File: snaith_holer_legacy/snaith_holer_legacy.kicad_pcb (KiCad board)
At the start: 2 copper layers, 30 x 30 mm, 24 parts, among them J1 Conn_02x08_Odd_Even, J10 Conn_01x01, J11 Conn_01x01, J12 Conn_01x01, J13 Conn_01x01, J14 Conn_01x01, J15 Conn_01x01, J16 Conn_01x01, J17 Conn_01x01, J18 Conn_01x01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

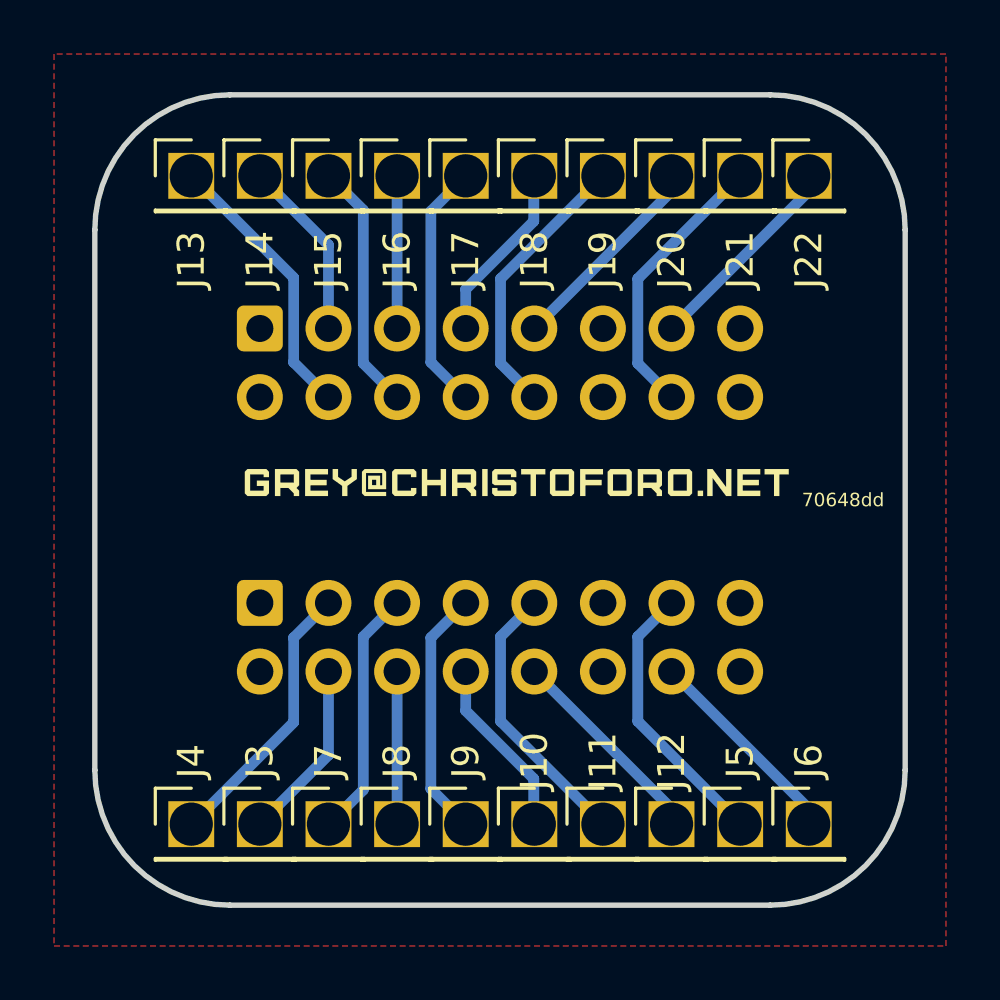
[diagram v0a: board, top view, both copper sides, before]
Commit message: make legacy substrate adapter pcbs
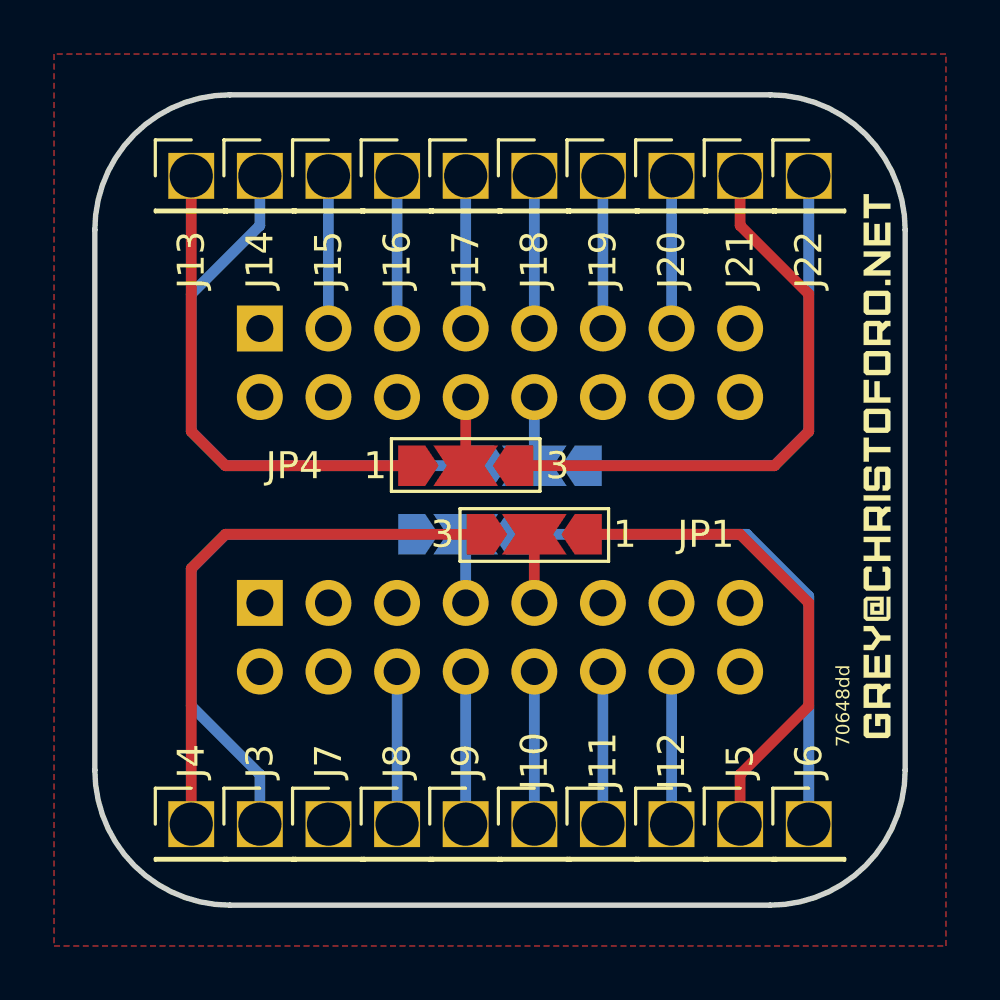
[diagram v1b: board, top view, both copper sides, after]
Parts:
- added JP1: SolderJumper_3_Bridged123, Jumper:SolderJumper-3_P2.0mm_Open_TrianglePad1.0x1.5mm_NumberLabels, F.Cu at (143.3, 95.4)
- added JP2: SolderJumper_3_Bridged123, Jumper:SolderJumper-3_P2.0mm_Open_TrianglePad1.0x1.5mm_NumberLabels, B.Cu at (140.7, 95.4)
- added JP3: SolderJumper_3_Bridged123, Jumper:SolderJumper-3_P2.0mm_Open_TrianglePad1.0x1.5mm_NumberLabels, B.Cu at (143.3, 92.9)
- added JP4: SolderJumper_3_Bridged123, Jumper:SolderJumper-3_P2.0mm_Open_TrianglePad1.0x1.5mm_NumberLabels, F.Cu at (140.7, 92.9)
- J1, J2: footprint custom:HIF3FC-16PA-2.54DSA(71) -> Connector_PinHeader_2.54mm:PinHeader_2x08_P2.54mm_Vertical
- moved SYM1 13.4 mm to (156.0, 92.9), turned to 90 degrees
- moved SYM2 13.4 mm to (156.0, 92.9), turned to 90 degrees
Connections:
- J1 pad 10: /V_5 -> /V_3
- J1 pad 12: unconnected-(J1-Pin_12-Pad12) -> /I_5
- J1 pad 13: /I_OD_B -> unconnected-(J1-Pin_13-Pad13)
- J1 pad 14: /V_OD_B -> /V_5
- J1 pad 3: /I_OD_T -> unconnected-(J1-Pin_3-Pad3)
- J1 pad 4: /V_OD_T -> /I_1
- J1 pad 5: /I_1 -> unconnected-(J1-Pin_5-Pad5)
- J1 pad 7: /I_3 -> /VB
- J1 pad 8: /V_3 -> /I_3
- J1 pad 9: /I_5 -> /IB
- J2 pad 10: /V_6 -> /IT
- J2 pad 11: unconnected-(J2-Pin_11-Pad11) -> /V_6
- J2 pad 13: /I_EV_B -> /I_6
- J2 pad 14: /V_EV_B -> unconnected-(J2-Pin_14-Pad14)
- J2 pad 3: /I_EV_T -> /V_2
- J2 pad 4: /V_EV_T -> unconnected-(J2-Pin_4-Pad4)
- J2 pad 6: /V_2 -> unconnected-(J2-Pin_6-Pad6)
- J2 pad 7: /I_4 -> /V_4
- J2 pad 8: /V_4 -> /VT
- J2 pad 9: /I_6 -> /I_4
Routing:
- net /I_EV_T: track 6.71 -> 21.7 mm
- net /V_OD_T: track 6.71 -> 19.2 mm
- net /V_OD_B: track 7.75 -> 20.1 mm
- net /V_EV_B: track 10.3 -> 21.7 mm
- net /I_OD_T: track 10.3 -> 20.7 mm
- net /I_EV_B: track 7.75 -> 18.1 mm
- net /I_1: track 9.23 -> 0.00 mm
- net /I_OD_B: track 10.3 -> 18.5 mm
- net /V_EV_T: track 10.3 -> 18.1 mm
- net /V_6: track 10.3 -> 5.65 mm
- net /I_5: track 10.3 -> 5.65 mm
- net /V_4: track 9.27 -> 5.65 mm
- net /I_3: track 9.27 -> 5.65 mm
- net /V_2: track 9.23 -> 5.65 mm
- net /VT: track 0.00 -> 2.54 mm
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
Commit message: upgrade contact checker with sense circuitry
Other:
- board text added: "0fe0217"
- board text removed: "70648dd"
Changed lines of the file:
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@@
     (effects (font (size 1 1) (thickness 0.15)) (justify mirror))
   )
-  (gr_text "70648dd" (at 154.7 101.76 90) (layer "B.SilkS")
+  (gr_text "0fe0217" (at 154.7 101.76 90) (layer "B.SilkS")
     (effects (font (size 0.5 0.5) (thickness 0.0625)) (justify mirror))
   )
@@
     (effects (font (size 1 1) (thickness 0.15)) (justify mirror))
   )
-  (gr_text "70648dd" (at 154.7 101.76 90) (layer "F.SilkS")
+  (gr_text "0fe0217" (at 154.7 101.76 90) (layer "F.SilkS")
     (effects (font (size 0.5 0.5) (thickness 0.0625)))
   )

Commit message: add some missing silkscreen
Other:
- board text added: "77a6489"
- board text removed: "0fe0217"
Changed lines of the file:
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@@
     (effects (font (size 1 1) (thickness 0.15)) (justify mirror))
   )
-  (gr_text "0fe0217" (at 154.7 101.76 90) (layer "B.SilkS")
-    (effects (font (size 0.5 0.5) (thickness 0.0625)) (justify mirror))
+  (gr_text "77a6489" (at 128.665 94.14 -90) (layer "B.SilkS")
+    (effects (font (size 1.5 1.5) (thickness 0.3) bold) (justify mirror))
   )
   (gr_text "2" (at 136.92 80.17 180) (layer "B.SilkS")
@@
     (effects (font (size 1 1) (thickness 0.15)) (justify mirror))
   )
-  (gr_text "0fe0217" (at 154.7 101.76 90) (layer "F.SilkS")
-    (effects (font (size 0.5 0.5) (thickness 0.0625)))
+  (gr_text "77a6489" (at 128.665 94.14 90) (layer "F.SilkS")
+    (effects (font (size 1.5 1.5) (thickness 0.3) bold))
   )
   (segment (start 130.57 106.14) (end 130.57 96.68) (width 0.4) (layer "F.Cu") (net 1))

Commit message: update silk
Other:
- board text added: "c5b4c2a"
- board text removed: "77a6489"
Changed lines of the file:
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@@
     (effects (font (size 1 1) (thickness 0.15)) (justify mirror))
   )
-  (gr_text "77a6489" (at 128.665 94.14 -90) (layer "B.SilkS")
+  (gr_text "c5b4c2a" (at 128.665 94.14 270) (layer "B.SilkS")
     (effects (font (size 1.5 1.5) (thickness 0.3) bold) (justify mirror))
   )
@@
     (effects (font (size 1 1) (thickness 0.15)) (justify mirror))
   )
-  (gr_text "77a6489" (at 128.665 94.14 90) (layer "F.SilkS")
+  (gr_text "c5b4c2a" (at 128.665 94.14 90) (layer "F.SilkS")
     (effects (font (size 1.5 1.5) (thickness 0.3) bold))
   )

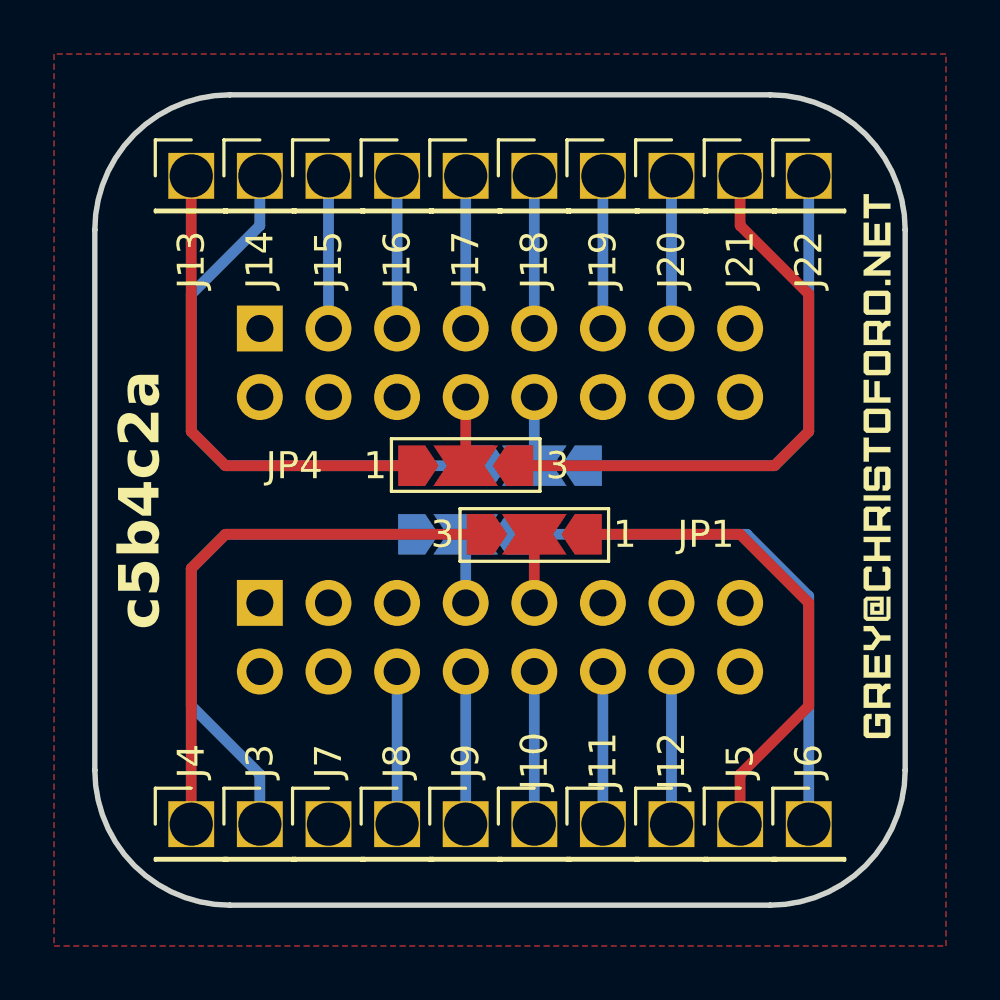
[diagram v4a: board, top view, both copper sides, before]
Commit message: fix missing trace
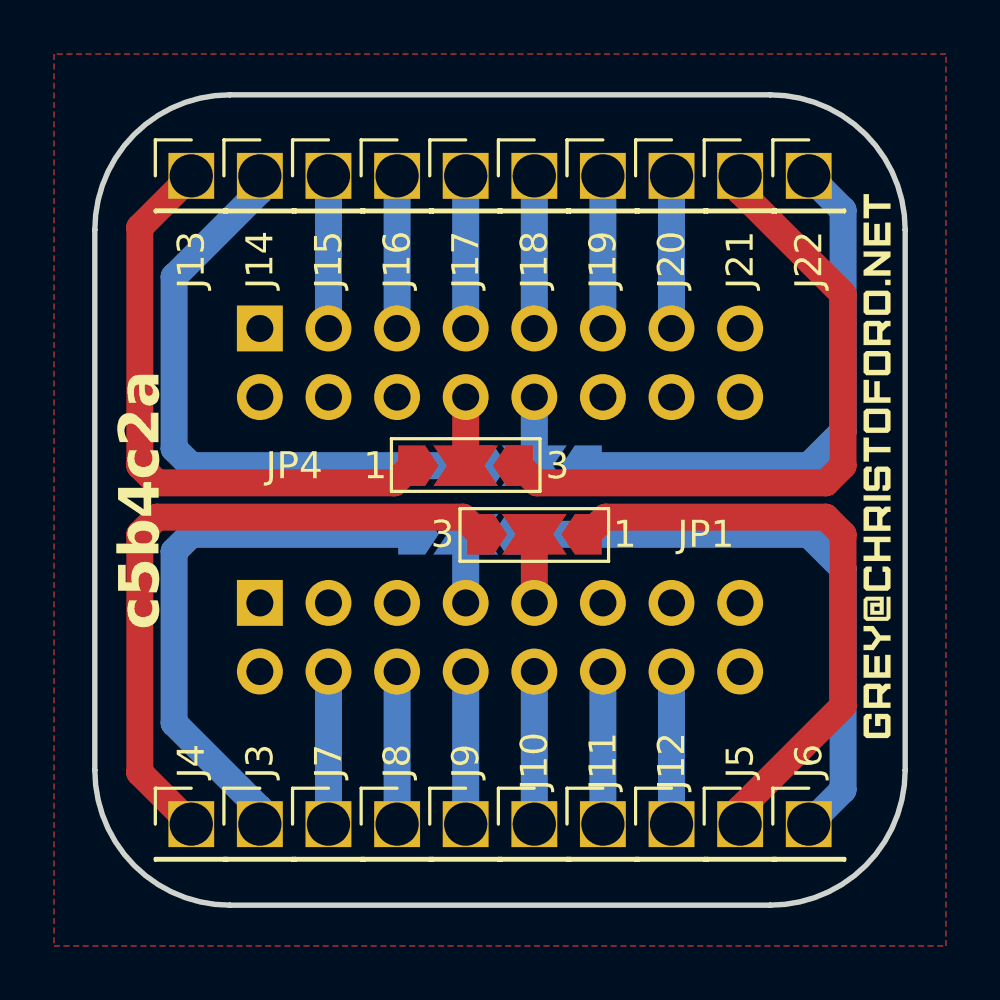
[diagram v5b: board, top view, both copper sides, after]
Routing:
- net /I_1: track 0.00 -> 5.65 mm
- net /V_EV_T: track 18.1 -> 22.1 mm
- net /I_OD_T: track 20.7 -> 24.7 mm
- net /I_OD_B: track 18.5 -> 22.3 mm
- net /V_EV_B: track 21.7 -> 24.8 mm
- net /V_OD_B: track 20.1 -> 22.5 mm
- net /I_EV_B: track 18.1 -> 19.9 mm
- net /V_OD_T: track 19.2 -> 20.5 mm
- net /I_EV_T: track 21.7 -> 23.0 mm
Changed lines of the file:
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@@
     (effects (font (size 1.5 1.5) (thickness 0.3) bold))
   )
-  (segment (start 130.57 106.14) (end 130.57 96.68) (width 0.4) (layer "F.Cu") (net 1))
-  (segment (start 130.57 96.68) (end 131.84 95.41) (width 0.4) (layer "F.Cu") (net 1))
-  (segment (start 131.84 95.41) (end 141.27 95.41) (width 0.4) (layer "F.Cu") (net 1))
-  (segment (start 130.57 101.76) (end 133.11 104.3) (width 0.4) (layer "B.Cu") (net 2))
-  (segment (start 138.73 95.41) (end 131.84 95.41) (width 0.4) (layer "B.Cu") (net 2))
-  (segment (start 133.11 104.3) (end 133.11 106.14) (width 0.4) (layer "B.Cu") (net 2))
-  (segment (start 131.84 95.41) (end 130.57 96.68) (width 0.4) (layer "B.Cu") (net 2))
-  (segment (start 130.57 96.68) (end 130.57 101.76) (width 0.4) (layer "B.Cu") (net 2))
-  (segment (start 138.19 100.49) (end 138.19 106.14) (width 0.4) (layer "B.Cu") (net 4))
-  (segment (start 140.73 100.49) (end 140.73 106.14) (width 0.4) (layer "B.Cu") (net 5))
-  (segment (start 143.27 106.14) (end 143.27 100.49) (width 0.4) (layer "B.Cu") (net 6))
-  (segment (start 145.81 100.49) (end 145.81 106.14) (width 0.4) (layer "B.Cu") (net 7))
-  (segment (start 148.35 106.14) (end 148.35 100.49) (width 0.4) (layer "B.Cu") (net 8))
-  (segment (start 153.43 97.95) (end 153.43 101.76) (width 0.4) (layer "F.Cu") (net 9))
-  (segment (start 153.43 101.76) (end 150.89 104.3) (width 0.4) (layer "F.Cu") (net 9))
-  (segment (start 150.89 104.3) (end 150.89 106.14) (width 0.4) (layer "F.Cu") (net 9))
-  (segment (start 150.89 95.41) (end 153.43 97.95) (width 0.4) (layer "F.Cu") (net 9))
-  (segment (start 145.27 95.41) (end 150.89 95.41) (width 0.4) (layer "F.Cu") (net 9))
-  (segment (start 151.138884 95.41) (end 153.43 97.701116) (width 0.4) (layer "B.Cu") (net 10))
-  (segment (start 142.73 95.41) (end 151.138884 95.41) (width 0.4) (layer "B.Cu") (net 10))
-  (segment (start 153.43 97.701116) (end 153.43 106.14) (width 0.4) (layer "B.Cu") (net 10))
-  (segment (start 133.11 83.98) (end 133.11 82.14) (width 0.4) (layer "B.Cu") (net 11))
-  (segment (start 131.84 92.87) (end 130.57 91.6) (width 0.4) (layer "B.Cu") (net 11))
-  (segment (start 141.27 92.87) (end 131.84 92.87) (width 0.4) (layer "B.Cu") (net 11))
-  (segment (start 130.57 91.6) (end 130.57 86.52) (width 0.4) (layer "B.Cu") (net 11))
-  (segment (start 130.57 86.52) (end 133.11 83.98) (width 0.4) (layer "B.Cu") (net 11))
-  (segment (start 131.84 92.87) (end 130.57 91.6) (width 0.4) (layer "F.Cu") (net 12))
-  (segment (start 130.57 91.6) (end 130.57 82.14) (width 0.4) (layer "F.Cu") (net 12))
-  (segment (start 138.73 92.87) (end 131.84 92.87) (width 0.4) (layer "F.Cu") (net 12))
-  (segment (start 138.19 82.14) (end 138.19 87.79) (width 0.4) (layer "B.Cu") (net 13))
-  (segment (start 135.65 82.14) (end 135.65 87.79) (width 0.4) (layer "B.Cu") (net 14))
-  (segment (start 143.27 82.14) (end 143.27 87.79) (width 0.4) (layer "B.Cu") (net 15))
-  (segment (start 140.73 82.14) (end 140.73 87.79) (width 0.4) (layer "B.Cu") (net 16))
-  (segment (start 148.35 82.14) (end 148.35 87.79) (width 0.4) (layer "B.Cu") (net 17))
-  (segment (start 145.81 82.14) (end 145.81 87.79) (width 0.4) (layer "B.Cu") (net 18))
-  (segment (start 152.16 92.87) (end 153.43 91.6) (width 0.4) (layer "B.Cu") (net 19))
-  (segment (start 153.43 91.6) (end 153.43 82.14) (width 0.4) (layer "B.Cu") (net 19))
-  (segment (start 145.27 92.87) (end 152.16 92.87) (width 0.4) (layer "B.Cu") (net 19))
-  (segment (start 153.43 86.52) (end 150.89 83.98) (width 0.4) (layer "F.Cu") (net 20))
-  (segment (start 142.73 92.87) (end 152.16 92.87) (width 0.4) (layer "F.Cu") (net 20))
-  (segment (start 150.89 83.98) (end 150.89 82.14) (width 0.4) (layer "F.Cu") (net 20))
-  (segment (start 152.16 92.87) (end 153.43 91.6) (width 0.4) (layer "F.Cu") (net 20))
-  (segment (start 153.43 91.6) (end 153.43 86.52) (width 0.4) (layer "F.Cu") (net 20))
-  (segment (start 140.73 95.41) (end 140.73 97.95) (width 0.4) (layer "B.Cu") (net 32))
-  (segment (start 143.27 95.41) (end 143.27 97.95) (width 0.4) (layer "F.Cu") (net 33))
-  (segment (start 140.73 92.87) (end 140.73 90.33) (width 0.4) (layer "F.Cu") (net 37))
-  (segment (start 143.27 92.87) (end 143.27 90.33) (width 0.4) (layer "B.Cu") (net 38))
+  (segment (start 141.27 95.41) (end 140.635 94.775) (width 1) (layer "F.Cu") (net 1))
+  (segment (start 140.635 94.775) (end 129.3 94.775) (width 1) (layer "F.Cu") (net 1))
+  (segment (start 129.3 94.775) (end 128.665 95.41) (width 1) (layer "F.Cu") (net 1))
+  (segment (start 128.665 104.235) (end 130.57 106.14) (width 1) (layer "F.Cu") (net 1))
+  (segment (start 128.665 95.41) (end 128.665 104.235) (width 1) (layer "F.Cu") (net 1))
+  (segment (start 129.935 102.395) (end 133.11 105.57) (width 1) (layer "B.Cu") (net 2))
+  (segment (start 133.11 105.57) (end 133.11 106.14) (width 1) (layer "B.Cu") (net 2))
+  (segment (start 129.935 96.045) (end 129.935 102.395) (width 1) (layer "B.Cu") (net 2))
+  (segment (start 138.73 95.41) (end 130.57 95.41) (width 1) (layer "B.Cu") (net 2))
+  (segment (start 130.57 95.41) (end 129.935 96.045) (width 1) (layer "B.Cu") (net 2))
+  (segment (start 135.65 106.14) (end 135.65 100.49) (width 1) (layer "B.Cu") (net 3))
+  (segment (start 138.19 100.49) (end 138.19 106.14) (width 1) (layer "B.Cu") (net 4))
+  (segment (start 140.73 106.14) (end 140.73 100.49) (width 1) (layer "B.Cu") (net 5))
+  (segment (start 143.27 100.49) (end 143.27 106.14) (width 1) (layer "B.Cu") (net 6))
+  (segment (start 145.81 106.14) (end 145.81 100.49) (width 1) (layer "B.Cu") (net 7))
+  (segment (start 148.35 100.49) (end 148.35 106.14) (width 1) (layer "B.Cu") (net 8))
+  (segment (start 154.7 95.41) (end 154.7 101.76) (width 1) (layer "F.Cu") (net 9))
+  (segment (start 154.7 101.76) (end 150.89 105.57) (width 1) (layer "F.Cu") (net 9))
+  (segment (start 145.27 95.41) (end 145.905 94.775) (width 1) (layer "F.Cu") (net 9))
+  (segment (start 145.905 94.775) (end 154.065 94.775) (width 1) (layer "F.Cu") (net 9))
+  (segment (start 150.89 105.57) (end 150.89 106.14) (width 1) (layer "F.Cu") (net 9))
+  (segment (start 154.065 94.775) (end 154.7 95.41) (width 1) (layer "F.Cu") (net 9))
+  (segment (start 142.73 95.41) (end 153.43 95.41) (width 1) (layer "B.Cu") (net 10))
+  (segment (start 154.7 96.68) (end 154.7 104.87) (width 1) (layer "B.Cu") (net 10))
+  (segment (start 153.43 95.41) (end 154.7 96.68) (width 1) (layer "B.Cu") (net 10))
+  (segment (start 154.7 104.87) (end 153.43 106.14) (width 1) (layer "B.Cu") (net 10))
+  (segment (start 133.11 82.7) (end 133.11 82.14) (width 1) (layer "B.Cu") (net 11))
+  (segment (start 130.57 92.87) (end 129.935 92.235) (width 1) (layer "B.Cu") (net 11))
+  (segment (start 129.935 85.875) (end 133.11 82.7) (width 1) (layer "B.Cu") (net 11))
+  (segment (start 141.27 92.87) (end 130.57 92.87) (width 1) (layer "B.Cu") (net 11))
+  (segment (start 129.935 92.235) (end 129.935 85.875) (width 1) (layer "B.Cu") (net 11))
+  (segment (start 138.73 92.87) (end 138.095 93.505) (width 1) (layer "F.Cu") (net 12))
+  (segment (start 128.665 92.87) (end 128.665 84.045) (width 1) (layer "F.Cu") (net 12))
+  (segment (start 129.3 93.505) (end 128.665 92.87) (width 1) (layer "F.Cu") (net 12))
+  (segment (start 128.665 84.045) (end 130.57 82.14) (width 1) (layer "F.Cu") (net 12))
+  (segment (start 138.095 93.505) (end 129.3 93.505) (width 1) (layer "F.Cu") (net 12))
+  (segment (start 138.19 87.79) (end 138.19 82.14) (width 1) (layer "B.Cu") (net 13))
+  (segment (start 135.65 82.14) (end 135.65 87.79) (width 1) (layer "B.Cu") (net 14))
+  (segment (start 143.27 87.79) (end 143.27 82.14) (width 1) (layer "B.Cu") (net 15))
+  (segment (start 140.73 82.14) (end 140.73 87.79) (width 1) (layer "B.Cu") (net 16))
+  (segment (start 148.35 87.79) (end 148.35 82.14) (width 1) (layer "B.Cu") (net 17))
+  (segment (start 145.81 82.14) (end 145.81 87.79) (width 1) (layer "B.Cu") (net 18))
+  (segment (start 154.7 91.6) (end 154.7 83.41) (width 1) (layer "B.Cu") (net 19))
+  (segment (start 145.27 92.87) (end 153.43 92.87) (width 1) (layer "B.Cu") (net 19))
+  (segment (start 154.7 83.41) (end 153.43 82.14) (width 1) (layer "B.Cu") (net 19))
+  (segment (start 153.43 92.87) (end 154.7 91.6) (width 1) (layer "B.Cu") (net 19))
+  (segment (start 142.73 92.87) (end 143.365 93.505) (width 1) (layer "F.Cu") (net 20))
+  (segment (start 154.7 92.87) (end 154.7 86.52) (width 1) (layer "F.Cu") (net 20))
+  (segment (start 154.7 86.52) (end 150.89 82.71) (width 1) (layer "F.Cu") (net 20))
+  (segment (start 150.89 82.71) (end 150.89 82.14) (width 1) (layer "F.Cu") (net 20))
+  (segment (start 154.065 93.505) (end 154.7 92.87) (width 1) (layer "F.Cu") (net 20))
+  (segment (start 143.365 93.505) (end 154.065 93.505) (width 1) (layer "F.Cu") (net 20))
+  (segment (start 140.73 97.95) (end 140.73 95.41) (width 1) (layer "B.Cu") (net 32))
+  (segment (start 143.27 95.41) (end 143.27 97.95) (width 1) (layer "F.Cu") (net 33))
+  (segment (start 140.73 92.87) (end 140.73 90.33) (width 1) (layer "F.Cu") (net 37))
+  (segment (start 143.27 92.87) (end 143.27 90.33) (width 1) (layer "B.Cu") (net 38))
   (zone (net 27) (net_name "GND") (layer "F.Cu") (hatch edge 0.5)
     (connect_pads (clearance 0.5))

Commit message: update silk
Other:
- board text added: "50b3ef0"
- board text removed: "c5b4c2a"
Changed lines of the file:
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@@
     (effects (font (size 1 1) (thickness 0.15)) (justify mirror))
   )
-  (gr_text "c5b4c2a" (at 128.665 94.14 270) (layer "B.SilkS")
+  (gr_text "50b3ef0" (at 128.665 94.14 270) (layer "B.SilkS")
     (effects (font (size 1.5 1.5) (thickness 0.3) bold) (justify mirror))
   )
@@
     (effects (font (size 1 1) (thickness 0.15)) (justify mirror))
   )
-  (gr_text "c5b4c2a" (at 128.665 94.14 90) (layer "F.SilkS")
+  (gr_text "50b3ef0" (at 128.665 94.14 90) (layer "F.SilkS")
     (effects (font (size 1.5 1.5) (thickness 0.3) bold))
   )
